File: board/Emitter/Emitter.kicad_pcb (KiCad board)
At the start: 2 copper layers, 15.5 x 94.5 mm, 17 parts, among them J1 Conn_01x02, Q1 2N3904, Q2 2N7000

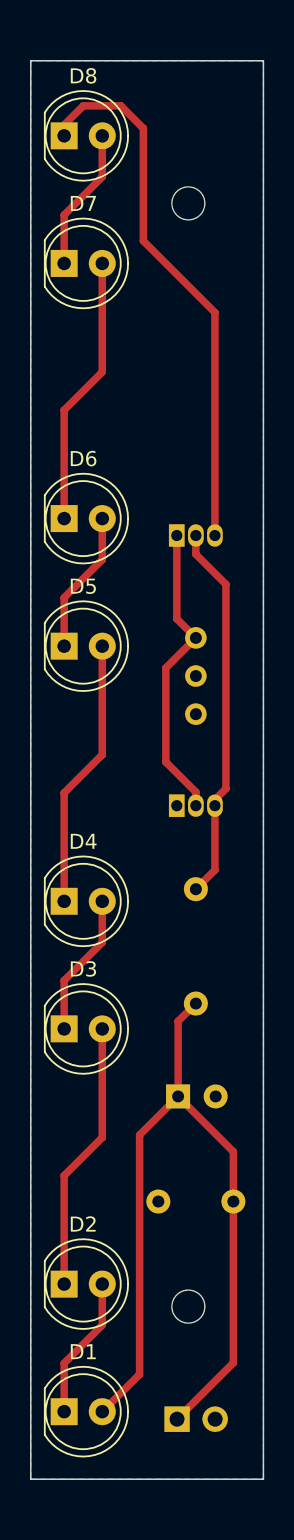
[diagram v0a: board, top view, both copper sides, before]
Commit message: Increase led and phototransistor spacing to better handle angled holes
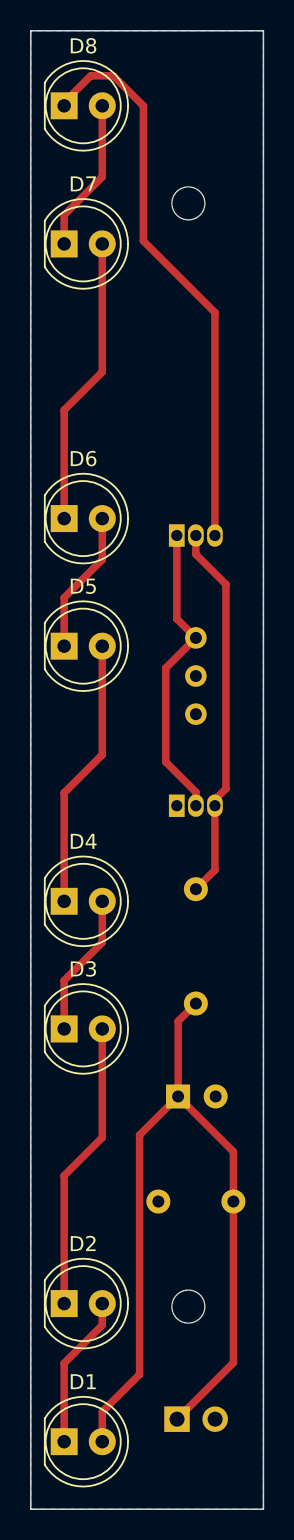
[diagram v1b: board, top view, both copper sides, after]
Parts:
- moved D1 2.00 mm to (138.7, 135.0)
- moved D8 2.00 mm to (138.7, 46.0)
- moved D2 1.30 mm to (138.7, 125.8)
- moved D7 1.30 mm to (138.7, 55.2)
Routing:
- net +12V: track 54.4 -> 56.4 mm
- net Net-(D8-Pad1): track 36.3 -> 37.7 mm
- net Net-(D6-Pad1): track 18.1 -> 19.4 mm
- net Net-(D2-Pad1): track 18.1 -> 19.4 mm
- net Net-(D7-Pad1): track 9.55 -> 10.3 mm
- net Net-(D1-Pad1): track 9.55 -> 10.3 mm
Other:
- board size 15.5 x 94.5 mm -> 15.5 x 98.5 mm
- board text added: "Saint Gimp Ballistic Chronograph Emitter 1.01"
- board text removed: "Saint Gimp Ballistic Chronograph Emitter 1.00"
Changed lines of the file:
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@@
     )
     (pad_to_mask_clearance 0)
-    (grid_origin 136.505 137.495)
+    (grid_origin 136.505 139.495)
     (pcbplotparams
       (layerselection 0x00010fc_ffffffff)
@@
   (net 12 "Net-(Q1-Pad3)")
   (footprint "LED_THT:LED_D5.0mm_IRGrey" (layer "F.Cu")
-    (at 138.73 124.495)
+    (at 138.73 125.795)
     (descr "LED, diameter 5.0mm, 2 pins, http://cdn-reichelt.de/documents/datenblatt/A500/LL-504BC2E-009.pdf")
     (tags "LED diameter 5.0mm 2 pins")
@@
   )
   (footprint "LED_THT:LED_D5.0mm_IRGrey" (layer "F.Cu")
-    (at 138.73 56.495)
+    (at 138.73 55.195)
     (descr "LED, diameter 5.0mm, 2 pins, http://cdn-reichelt.de/documents/datenblatt/A500/LL-504BC2E-009.pdf")
     (tags "LED diameter 5.0mm 2 pins")
@@
   )
   (footprint "LED_THT:LED_D5.0mm_IRGrey" (layer "F.Cu")
-    (at 138.73 47.995)
+    (at 138.73 45.995)
     (descr "LED, diameter 5.0mm, 2 pins, http://cdn-reichelt.de/documents/datenblatt/A500/LL-504BC2E-009.pdf")
     (tags "LED diameter 5.0mm 2 pins")
@@
   )
   (footprint "LED_THT:LED_D5.0mm_IRGrey" (layer "F.Cu")
-    (at 138.73 132.995)
+    (at 138.73 134.995)
     (descr "LED, diameter 5.0mm, 2 pins, http://cdn-reichelt.de/documents/datenblatt/A500/LL-504BC2E-009.pdf")
     (tags "LED diameter 5.0mm 2 pins")
@@
     )
   )
-  (gr_rect (start 136.505 137.495) (end 152.005 42.995) (layer "Edge.Cuts") (width 0.1) (fill none))
-  (gr_text "Saint Gimp\nBallistic\nChronograph\nEmitter 1.00" (at 147.505 62.995 270) (layer "B.SilkS")
+  (gr_rect (start 136.505 139.495) (end 152.005 40.995) (layer "Edge.Cuts") (width 0.1) (fill none))
+  (gr_text "Saint Gimp\nBallistic\nChronograph\nEmitter 1.01" (at 147.505 62.995 270) (layer "B.SilkS")
     (effects (font (size 1 1) (thickness 0.15)) (justify mirror))
   )
@@
   )
   (segment (start 150.005 118.995) (end 150.005 115.677379) (width 0.5) (layer "F.Cu") (net 1))
+  (segment (start 141.27 132.995) (end 141.27 134.995) (width 0.5) (layer "F.Cu") (net 1))
   (segment (start 146.322621 106.987379) (end 147.505 105.805) (width 0.5) (layer "F.Cu") (net 1))
   (segment (start 146.25 133.495) (end 150.005 129.74) (width 0.5) (layer "F.Cu") (net 1))
@@
   (segment (start 146.322621 111.995) (end 146.322621 106.987379) (width 0.5) (layer "F.Cu") (net 1))
   (segment (start 150.005 115.677379) (end 146.322621 111.995) (width 0.5) (layer "F.Cu") (net 1))
-  (segment (start 138.73 132.995) (end 138.73 129.77) (width 0.5) (layer "F.Cu") (net 3))
-  (segment (start 141.27 127.23) (end 141.27 124.495) (width 0.5) (layer "F.Cu") (net 3))
-  (segment (start 138.73 129.77) (end 141.27 127.23) (width 0.5) (layer "F.Cu") (net 3))
+  (segment (start 141.27 127.23) (end 138.73 129.77) (width 0.5) (layer "F.Cu") (net 3))
+  (segment (start 141.27 125.795) (end 141.27 127.23) (width 0.5) (layer "F.Cu") (net 3))
+  (segment (start 138.73 129.77) (end 138.73 134.995) (width 0.5) (layer "F.Cu") (net 3))
   (segment (start 138.73 117.27) (end 141.27 114.73) (width 0.5) (layer "F.Cu") (net 4))
-  (segment (start 138.73 124.495) (end 138.73 117.27) (width 0.5) (layer "F.Cu") (net 4))
+  (segment (start 138.73 125.795) (end 138.73 117.27) (width 0.5) (layer "F.Cu") (net 4))
   (segment (start 141.27 114.73) (end 141.27 107.495) (width 0.5) (layer "F.Cu") (net 4))
   (segment (start 141.27 101.73) (end 141.27 98.995) (width 0.5) (layer "F.Cu") (net 5))
@@
   (segment (start 138.73 78.77) (end 141.27 76.23) (width 0.5) (layer "F.Cu") (net 7))
   (segment (start 138.73 81.995) (end 138.73 78.77) (width 0.5) (layer "F.Cu") (net 7))
+  (segment (start 141.27 63.73) (end 141.27 55.195) (width 0.5) (layer "F.Cu") (net 8))
+  (segment (start 138.73 73.495) (end 138.73 66.27) (width 0.5) (layer "F.Cu") (net 8))
   (segment (start 138.73 66.27) (end 141.27 63.73) (width 0.5) (layer "F.Cu") (net 8))
-  (segment (start 141.27 63.73) (end 141.27 56.495) (width 0.5) (layer "F.Cu") (net 8))
-  (segment (start 138.73 73.495) (end 138.73 66.27) (width 0.5) (layer "F.Cu") (net 8))
+  (segment (start 138.73 55.195) (end 138.73 53.27) (width 0.5) (layer "F.Cu") (net 9))
   (segment (start 138.73 53.27) (end 141.27 50.73) (width 0.5) (layer "F.Cu") (net 9))
-  (segment (start 141.27 50.73) (end 141.27 47.995) (width 0.5) (layer "F.Cu") (net 9))
-  (segment (start 138.73 56.495) (end 138.73 53.27) (width 0.5) (layer "F.Cu") (net 9))
-  (segment (start 140.005 45.995) (end 142.505 45.995) (width 0.5) (layer "F.Cu") (net 10))
-  (segment (start 138.73 47.995) (end 138.73 47.27) (width 0.5) (layer "F.Cu") (net 10))
-  (segment (start 138.73 47.27) (end 140.005 45.995) (width 0.5) (layer "F.Cu") (net 10))
-  (segment (start 144.005 54.995) (end 144.005 47.495) (width 0.5) (layer "F.Cu") (net 10))
+  (segment (start 141.27 50.73) (end 141.27 45.995) (width 0.5) (layer "F.Cu") (net 9))
+  (segment (start 142.005 43.995) (end 140.505 43.995) (width 0.5) (layer "F.Cu") (net 10))
+  (segment (start 148.775 74.6225) (end 148.775 59.765) (width 0.5) (layer "F.Cu") (net 10))
+  (segment (start 144.005 45.995) (end 142.005 43.995) (width 0.5) (layer "F.Cu") (net 10))
+  (segment (start 140.505 43.995) (end 138.73 45.77) (width 0.5) (layer "F.Cu") (net 10))
+  (segment (start 138.73 45.77) (end 138.73 45.995) (width 0.5) (layer "F.Cu") (net 10))
+  (segment (start 144.005 54.995) (end 144.005 45.995) (width 0.5) (layer "F.Cu") (net 10))
   (segment (start 148.775 59.765) (end 144.005 54.995) (width 0.5) (layer "F.Cu") (net 10))
-  (segment (start 144.005 47.495) (end 142.505 45.995) (width 0.5) (layer "F.Cu") (net 10))
-  (segment (start 148.775 74.6225) (end 148.775 59.765) (width 0.5) (layer "F.Cu") (net 10))
   (segment (start 146.235 80.175) (end 146.235 74.6225) (width 0.5) (layer "F.Cu") (net 11))
   (segment (start 145.505 83.445) (end 147.505 81.445) (width 0.5) (layer "F.Cu") (net 11))
@@
     (polygon
       (pts
-        (xy 136.505 137.495)
-        (xy 152.005 137.495)
-        (xy 152.005 42.995)
-        (xy 136.505 42.995)
+        (xy 136.505 139.495)
+        (xy 152.005 139.495)
+        (xy 152.005 40.995)
+        (xy 136.505 40.995)
       )
     )

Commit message: Detector changes to better control overall bias level
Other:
- board text added: "Saint Gimp Ballistic Chronograph Emitter 1.0.1"
- board text removed: "Saint Gimp Ballistic Chronograph Emitter 1.01"
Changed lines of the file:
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@@
   )
   (gr_rect (start 136.505 139.495) (end 152.005 40.995) (layer "Edge.Cuts") (width 0.1) (fill none))
-  (gr_text "Saint Gimp\nBallistic\nChronograph\nEmitter 1.01" (at 147.505 62.995 270) (layer "B.SilkS")
+  (gr_text "Saint Gimp\nBallistic\nChronograph\nEmitter 1.0.1" (at 147.505 62.995 270) (layer "B.SilkS")
     (effects (font (size 1 1) (thickness 0.15)) (justify mirror))
   )

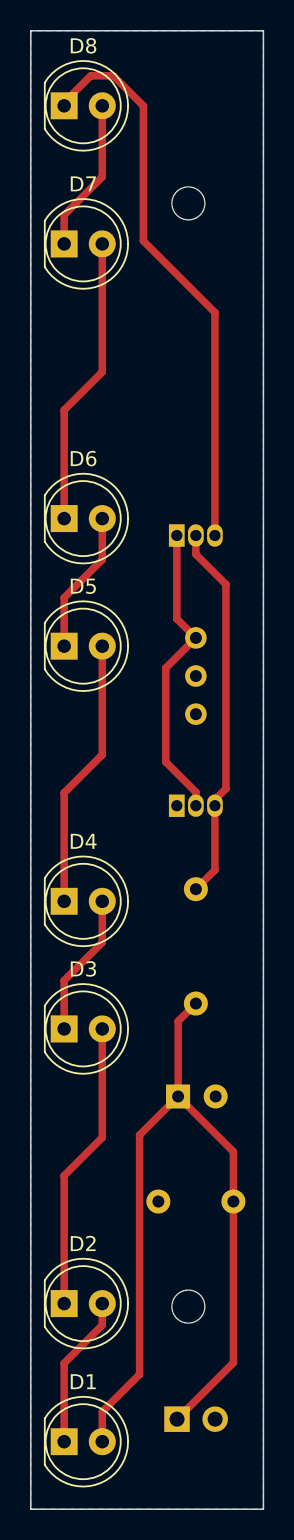
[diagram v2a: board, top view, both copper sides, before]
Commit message: Changed connectors, 3D models, added test points
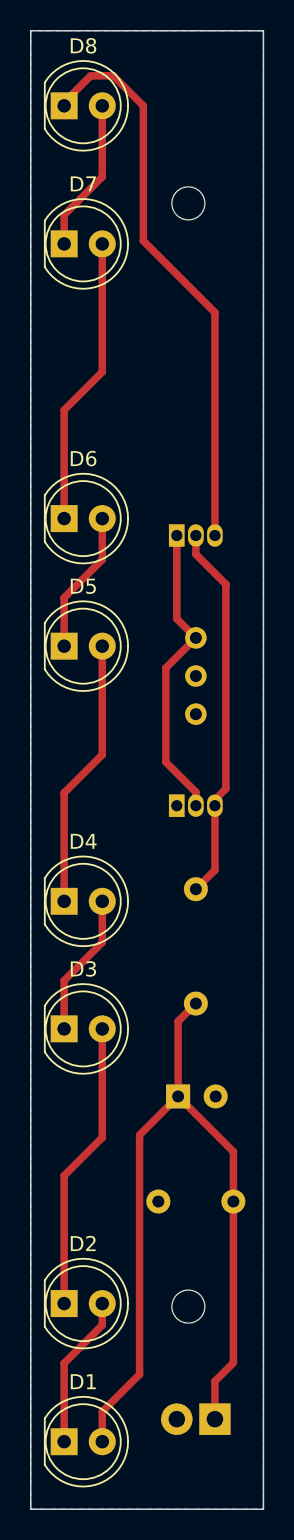
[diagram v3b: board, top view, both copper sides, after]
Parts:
- D1, D2, D3, D4, D5, D6, D7, D8: value LED -> OP294
- J1: footprint SaintGimp:KF2510_Header_1x02_Vertical -> TerminalBlock_TE-Connectivity:TerminalBlock_TE_282834-2_1x02_P2.54mm_Horizontal
- moved J1 2.53 mm to (148.8, 133.5), turned to 180 degrees
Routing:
- net +12V: track 56.4 -> 55.3 mm
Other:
- board text added: "14V"
- board text added: "Saint Gimp Ballistic Chronograph Emitter 1.1.0"
- board text removed: "12V"
- board text removed: "Saint Gimp Ballistic Chronograph Emitter 1.0.1"

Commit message: Update silkscreen on emitter
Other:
- board text added: "15V"
- board text added: "Saint Gimp Ballistic Chronograph Emitter 1.1.1"
- board text removed: "14V"
- board text removed: "Saint Gimp Ballistic Chronograph Emitter 1.1.0"
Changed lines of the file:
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@@
   )
   (gr_rect (start 136.505 139.495) (end 152.005 40.995) (layer "Edge.Cuts") (width 0.1) (fill none))
-  (gr_text "Saint Gimp\nBallistic\nChronograph\nEmitter 1.1.0" (at 147.505 62.995 270) (layer "B.SilkS")
+  (gr_text "Saint Gimp\nBallistic\nChronograph\nEmitter 1.1.1" (at 147.505 62.995 270) (layer "B.SilkS")
     (effects (font (size 1 1) (thickness 0.15)) (justify mirror))
   )
@@
     (effects (font (size 1 1) (thickness 0.15)) (justify mirror))
   )
-  (gr_text "14V" (at 149.505 138.495) (layer "B.SilkS")
+  (gr_text "15V" (at 149.505 138.495) (layer "B.SilkS")
     (effects (font (size 1 1) (thickness 0.15)) (justify mirror))
   )
